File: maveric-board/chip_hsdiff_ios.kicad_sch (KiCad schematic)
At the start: 1 part, among them U1 Socket

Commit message: reannotate, fix all ERCs
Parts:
- renumbered U1 to U3
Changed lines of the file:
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@@
 		(dnp no)
 		(fields_autoplaced yes)
-		(property "Reference" "U1"
+		(property "Reference" "U3"
 			(at 134.62 17.78 0)
 			(effects
@@
 			(project ""
 				(path "/ae861d46-65fb-4872-932f-ad48addb0154/d741604b-a788-4cfa-8679-fc6e466b5431"
-					(reference "U1")
+					(reference "U3")
 					(unit 2)
 				)
@@
 		(dnp no)
 		(fields_autoplaced yes)
-		(property "Reference" "U1"
+		(property "Reference" "U3"
 			(at 54.61 17.78 0)
 			(effects
@@
 			(project ""
 				(path "/ae861d46-65fb-4872-932f-ad48addb0154/d741604b-a788-4cfa-8679-fc6e466b5431"
-					(reference "U1")
+					(reference "U3")
 					(unit 1)
 				)
@@
 		(dnp no)
 		(fields_autoplaced yes)
-		(property "Reference" "U1"
+		(property "Reference" "U3"
 			(at 134.62 104.14 0)
 			(effects
@@
 			(project ""
 				(path "/ae861d46-65fb-4872-932f-ad48addb0154/d741604b-a788-4cfa-8679-fc6e466b5431"
-					(reference "U1")
+					(reference "U3")
 					(unit 4)
 				)
@@
 		(dnp no)
 		(fields_autoplaced yes)
-		(property "Reference" "U1"
+		(property "Reference" "U3"
 			(at 222.25 17.78 0)
 			(effects
@@
 			(project ""
 				(path "/ae861d46-65fb-4872-932f-ad48addb0154/d741604b-a788-4cfa-8679-fc6e466b5431"
-					(reference "U1")
+					(reference "U3")
 					(unit 3)
 				)

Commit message: add uni2 socket footprint, check against drawing, fix npth, assign all footprints and part numbers
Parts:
- U3: footprint (none) -> maveric-parts:BGA-1733-.92-47.725x47.725
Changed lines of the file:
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@@
 			)
 		)
-		(property "Footprint" ""
+		(property "Footprint" "maveric-parts:BGA-1733-.92-47.725x47.725"
 			(at 96.52 24.13 0)
 			(effects
@@
 			)
 		)
-		(property "Footprint" ""
+		(property "Footprint" "maveric-parts:BGA-1733-.92-47.725x47.725"
 			(at 16.51 24.13 0)
 			(effects
@@
 			)
 		)
-		(property "Footprint" ""
+		(property "Footprint" "maveric-parts:BGA-1733-.92-47.725x47.725"
 			(at 96.52 110.49 0)
 			(effects
@@
 			)
 		)
-		(property "Footprint" ""
+		(property "Footprint" "maveric-parts:BGA-1733-.92-47.725x47.725"
 			(at 184.15 24.13 0)
 			(effects

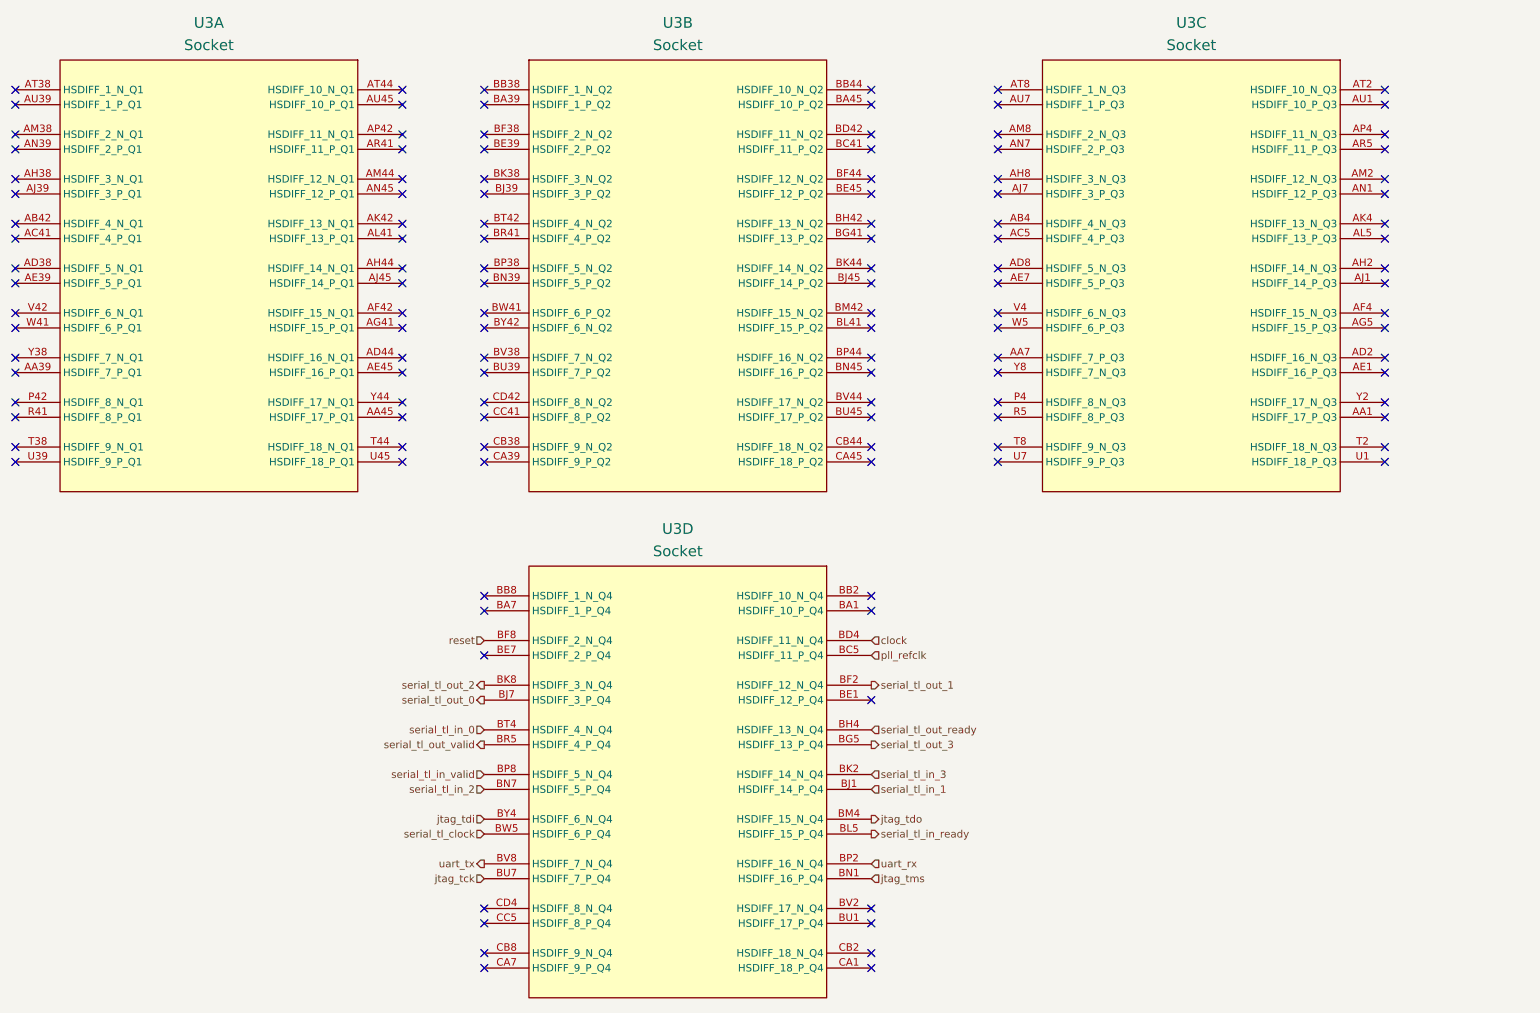
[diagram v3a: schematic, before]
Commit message: some docs + dnp uni2 socket
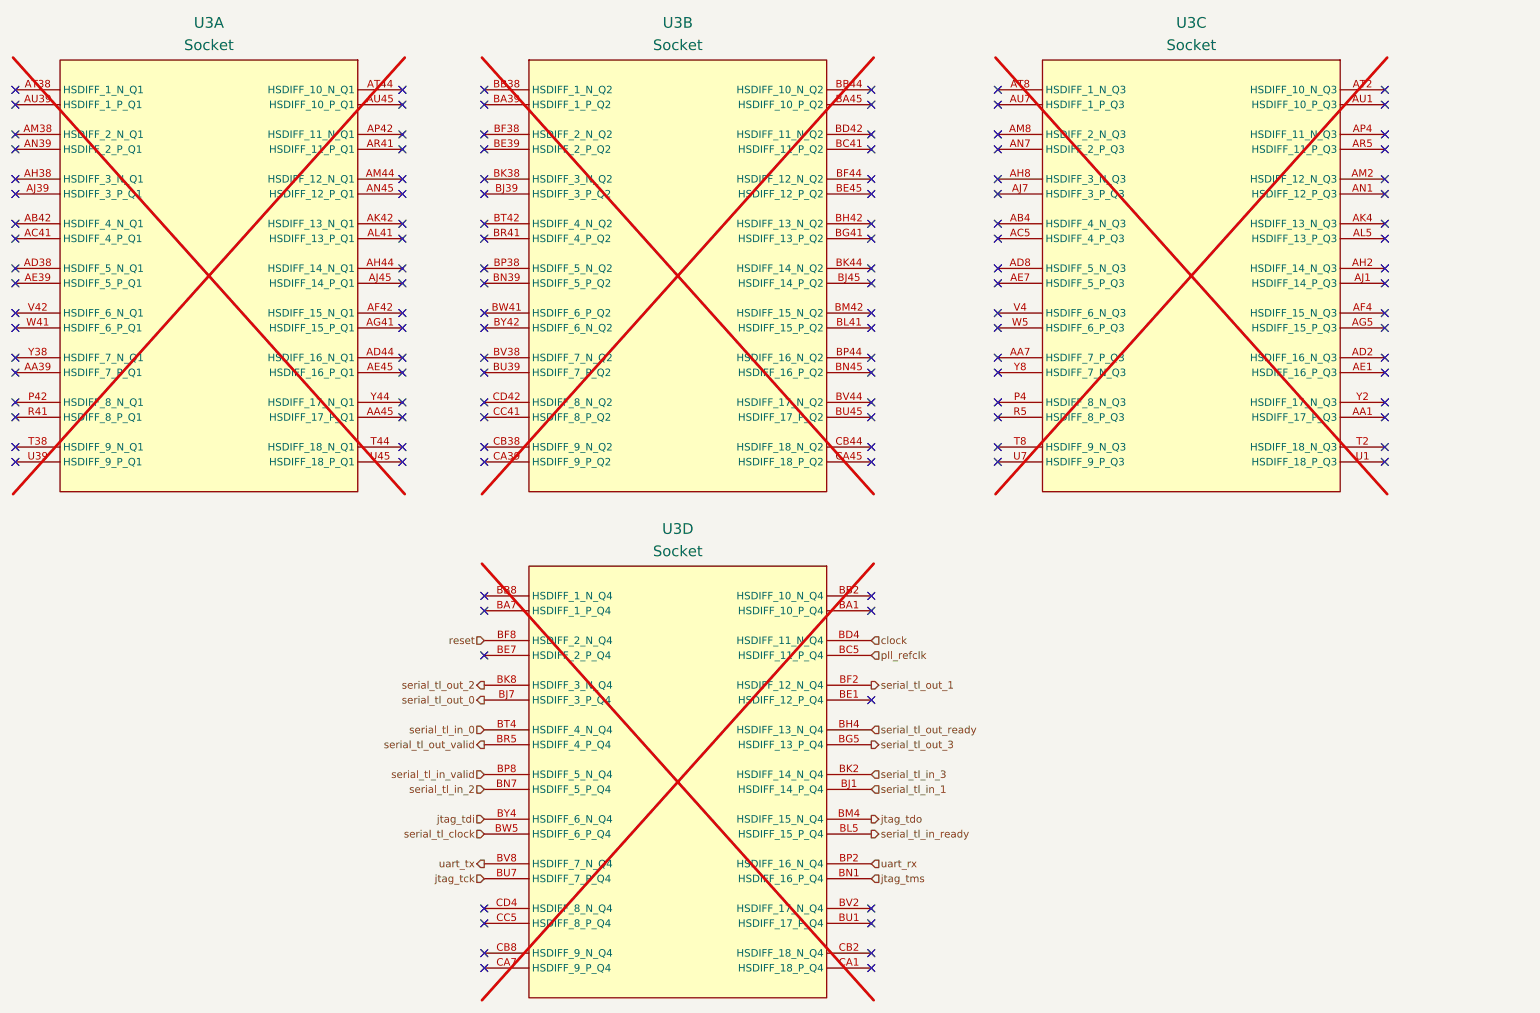
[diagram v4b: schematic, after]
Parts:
- U3: now not fitted
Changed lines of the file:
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@@
 		(in_bom yes)
 		(on_board yes)
-		(dnp no)
+		(dnp yes)
 		(fields_autoplaced yes)
 		(property "Reference" "U3"
@@
 		(in_bom yes)
 		(on_board yes)
-		(dnp no)
+		(dnp yes)
 		(fields_autoplaced yes)
 		(property "Reference" "U3"
@@
 		(in_bom yes)
 		(on_board yes)
-		(dnp no)
+		(dnp yes)
 		(fields_autoplaced yes)
 		(property "Reference" "U3"
@@
 		(in_bom yes)
 		(on_board yes)
-		(dnp no)
+		(dnp yes)
 		(fields_autoplaced yes)
 		(property "Reference" "U3"

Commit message: fix bump mapping
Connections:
- net clock: now also U3.AP4 (HSDIFF_11_N_Q3); no longer U3.BD4 (HSDIFF_11_N_Q4)
- net jtag_tck: now also U3.AA7 (HSDIFF_7_P_Q3); no longer U3.BU7 (HSDIFF_7_P_Q4)
- net jtag_tdi: now also U3.V4 (HSDIFF_6_N_Q3); no longer U3.BY4 (HSDIFF_6_N_Q4)
- net jtag_tdo: now also U3.AF4 (HSDIFF_15_N_Q3); no longer U3.BM4 (HSDIFF_15_N_Q4)
- net jtag_tms: now also U3.AE1 (HSDIFF_16_P_Q3); no longer U3.BN1 (HSDIFF_16_P_Q4)
- net pll_refclk: now also U3.AR5 (HSDIFF_11_P_Q3); no longer U3.BC5 (HSDIFF_11_P_Q4)
- net reset: now also U3.AM8 (HSDIFF_2_N_Q3); no longer U3.BF8 (HSDIFF_2_N_Q4)
- net serial_tl_clock: now also U3.W5 (HSDIFF_6_P_Q3); no longer U3.BW5 (HSDIFF_6_P_Q4)
- net serial_tl_in_0: now also U3.AB4 (HSDIFF_4_N_Q3); no longer U3.BT4 (HSDIFF_4_N_Q4)
- net serial_tl_in_1: now also U3.AJ1 (HSDIFF_14_P_Q3); no longer U3.BJ1 (HSDIFF_14_P_Q4)
- net serial_tl_in_2: now also U3.AE7 (HSDIFF_5_P_Q3); no longer U3.BN7 (HSDIFF_5_P_Q4)
- net serial_tl_in_3: now also U3.AH2 (HSDIFF_14_N_Q3); no longer U3.BK2 (HSDIFF_14_N_Q4)
- net serial_tl_in_ready: now also U3.AG5 (HSDIFF_15_P_Q3); no longer U3.BL5 (HSDIFF_15_P_Q4)
- net serial_tl_in_valid: now also U3.AD8 (HSDIFF_5_N_Q3); no longer U3.BP8 (HSDIFF_5_N_Q4)
- net serial_tl_out_0: now also U3.AJ7 (HSDIFF_3_P_Q3); no longer U3.BJ7 (HSDIFF_3_P_Q4)
- net serial_tl_out_1: now also U3.AM2 (HSDIFF_12_N_Q3); no longer U3.BF2 (HSDIFF_12_N_Q4)
- net serial_tl_out_2: now also U3.AH8 (HSDIFF_3_N_Q3); no longer U3.BK8 (HSDIFF_3_N_Q4)
- net serial_tl_out_3: now also U3.AL5 (HSDIFF_13_P_Q3); no longer U3.BG5 (HSDIFF_13_P_Q4)
- net serial_tl_out_ready: now also U3.AK4 (HSDIFF_13_N_Q3); no longer U3.BH4 (HSDIFF_13_N_Q4)
- net serial_tl_out_valid: now also U3.AC5 (HSDIFF_4_P_Q3); no longer U3.BR5 (HSDIFF_4_P_Q4)
- net uart_rx: now also U3.AD2 (HSDIFF_16_N_Q3); no longer U3.BP2 (HSDIFF_16_N_Q4)
- net uart_tx: now also U3.Y8 (HSDIFF_7_N_Q3); no longer U3.BV8 (HSDIFF_7_N_Q4)

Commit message: resync all symbols to schematic, reannotate schematic
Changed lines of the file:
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@@
 	(hierarchical_label "uart_tx"
 		(shape output)
+		(at 189.23 74.93 180)
+		(fields_autoplaced yes)
+		(effects
+			(font
+				(size 1.27 1.27)
+			)
+			(justify right)
+		)
+	)
+	(hierarchical_label "serial_tl_in_3"
+		(shape input)
+		(at 255.27 59.69 0)
+		(fields_autoplaced yes)
+		(effects
+			(font
+				(size 1.27 1.27)
+			)
+			(justify left)
+		)
+	)
+	(hierarchical_label "serial_tl_out_3"
+		(shape output)
+		(at 255.27 54.61 0)
+		(fields_autoplaced yes)
+		(effects
+			(font
+				(size 1.27 1.27)
+			)
+			(justify left)
+		)
+	)
+	(hierarchical_label "jtag_tdi"
+		(shape input)
+		(at 189.23 67.31 180)
+		(fields_autoplaced yes)
+		(effects
+			(font
+				(size 1.27 1.27)
+			)
+			(justify right)
+		)
+	)
+	(hierarchical_label "serial_tl_in_ready"
+		(shape output)
+		(at 255.27 69.85 0)
+		(fields_autoplaced yes)
+		(effects
+			(font
+				(size 1.27 1.27)
+			)
+			(justify left)
+		)
+	)
+	(hierarchical_label "serial_tl_out_0"
+		(shape output)
+		(at 189.23 46.99 180)
+		(fields_autoplaced yes)
+		(effects
+			(font
+				(size 1.27 1.27)
+			)
+			(justify right)
+		)
+	)
+	(hierarchical_label "serial_tl_in_2"
+		(shape input)
+		(at 189.23 62.23 180)
+		(fields_autoplaced yes)
+		(effects
+			(font
+				(size 1.27 1.27)
+			)
+			(justify right)
+		)
+	)
+	(hierarchical_label "serial_tl_out_valid"
+		(shape output)
+		(at 189.23 54.61 180)
+		(fields_autoplaced yes)
+		(effects
+			(font
+				(size 1.27 1.27)
+			)
+			(justify right)
+		)
+	)
+	(hierarchical_label "serial_tl_out_ready"
+		(shape input)
+		(at 255.27 52.07 0)
+		(fields_autoplaced yes)
+		(effects
+			(font
+				(size 1.27 1.27)
+			)
+			(justify left)
+		)
+	)
+	(hierarchical_label "reset"
+		(shape input)
+		(at 189.23 36.83 180)
+		(fields_autoplaced yes)
+		(effects
+			(font
+				(size 1.27 1.27)
+			)
+			(justify right)
+		)
+	)
+	(hierarchical_label "jtag_tms"
+		(shape input)
+		(at 255.27 77.47 0)
+		(fields_autoplaced yes)
+		(effects
+			(font
+				(size 1.27 1.27)
+			)
+			(justify left)
+		)
+	)
+	(hierarchical_label "serial_tl_out_2"
+		(shape output)
+		(at 189.23 44.45 180)
+		(fields_autoplaced yes)
+		(effects
+			(font
+				(size 1.27 1.27)
+			)
+			(justify right)
+		)
+	)
+	(hierarchical_label "serial_tl_clock"
+		(shape input)
+		(at 189.23 69.85 180)
+		(fields_autoplaced yes)
+		(effects
+			(font
+				(size 1.27 1.27)
+			)
+			(justify right)
+		)
+	)
+	(hierarchical_label "serial_tl_in_valid"
+		(shape input)
+		(at 189.23 59.69 180)
+		(fields_autoplaced yes)
+		(effects
+			(font
+				(size 1.27 1.27)
+			)
+			(justify right)
+		)
+	)
+	(hierarchical_label "uart_rx"
+		(shape input)
+		(at 255.27 74.93 0)
+		(fields_autoplaced yes)
+		(effects
+			(font
+				(size 1.27 1.27)
+			)
+			(justify left)
+		)
+	)
+	(hierarchical_label "serial_tl_in_0"
+		(shape input)
+		(at 189.23 52.07 180)
+		(fields_autoplaced yes)
+		(effects
+			(font
+				(size 1.27 1.27)
+			)
+			(justify right)
+		)
+	)
+	(hierarchical_label "serial_tl_in_1"
+		(shape input)
+		(at 255.27 62.23 0)
+		(fields_autoplaced yes)
+		(effects
+			(font
+				(size 1.27 1.27)
+			)
+			(justify left)
+		)
+	)
+	(hierarchical_label "pll_refclk"
+		(shape input)
+		(at 255.27 39.37 0)
+		(fields_autoplaced yes)
+		(effects
+			(font
+				(size 1.27 1.27)
+			)
+			(justify left)
+		)
+	)
+	(hierarchical_label "jtag_tck"
+		(shape input)
 		(at 189.23 77.47 180)
 		(fields_autoplaced yes)
 		(effects
-			(font
-				(size 1.27 1.27)
-			)
-			(justify right)
-		)
-	)
-	(hierarchical_label "serial_tl_in_3"
-		(shape input)
-		(at 255.27 59.69 0)
-		(fields_autoplaced yes)
-		(effects
-			(font
-				(size 1.27 1.27)
-			)
-			(justify left)
-		)
-	)
-	(hierarchical_label "serial_tl_out_3"
-		(shape output)
-		(at 255.27 54.61 0)
-		(fields_autoplaced yes)
-		(effects
-			(font
-				(size 1.27 1.27)
-			)
-			(justify left)
-		)
-	)
-	(hierarchical_label "jtag_tdi"
-		(shape input)
-		(at 189.23 67.31 180)
-		(fields_autoplaced yes)
-		(effects
-			(font
-				(size 1.27 1.27)
-			)
-			(justify right)
-		)
-	)
-	(hierarchical_label "serial_tl_in_ready"
-		(shape output)
-		(at 255.27 69.85 0)
-		(fields_autoplaced yes)
-		(effects
-			(font
-				(size 1.27 1.27)
-			)
-			(justify left)
-		)
-	)
-	(hierarchical_label "serial_tl_out_0"
-		(shape output)
-		(at 189.23 46.99 180)
-		(fields_autoplaced yes)
-		(effects
-			(font
-				(size 1.27 1.27)
-			)
-			(justify right)
-		)
-	)
-	(hierarchical_label "serial_tl_in_2"
-		(shape input)
-		(at 189.23 62.23 180)
-		(fields_autoplaced yes)
-		(effects
-			(font
-				(size 1.27 1.27)
-			)
-			(justify right)
-		)
-	)
-	(hierarchical_label "serial_tl_out_valid"
-		(shape output)
-		(at 189.23 54.61 180)
-		(fields_autoplaced yes)
-		(effects
-			(font
-				(size 1.27 1.27)
-			)
-			(justify right)
-		)
-	)
-	(hierarchical_label "serial_tl_out_ready"
-		(shape input)
-		(at 255.27 52.07 0)
-		(fields_autoplaced yes)
-		(effects
-			(font
-				(size 1.27 1.27)
-			)
-			(justify left)
-		)
-	)
-	(hierarchical_label "reset"
-		(shape input)
-		(at 189.23 36.83 180)
-		(fields_autoplaced yes)
-		(effects
-			(font
-				(size 1.27 1.27)
-			)
-			(justify right)
-		)
-	)
-	(hierarchical_label "jtag_tms"
-		(shape input)
-		(at 255.27 77.47 0)
-		(fields_autoplaced yes)
-		(effects
-			(font
-				(size 1.27 1.27)
-			)
-			(justify left)
-		)
-	)
-	(hierarchical_label "serial_tl_out_2"
-		(shape output)
-		(at 189.23 44.45 180)
-		(fields_autoplaced yes)
-		(effects
-			(font
-				(size 1.27 1.27)
-			)
-			(justify right)
-		)
-	)
-	(hierarchical_label "serial_tl_clock"
-		(shape input)
-		(at 189.23 69.85 180)
-		(fields_autoplaced yes)
-		(effects
-			(font
-				(size 1.27 1.27)
-			)
-			(justify right)
-		)
-	)
-	(hierarchical_label "serial_tl_in_valid"
-		(shape input)
-		(at 189.23 59.69 180)
-		(fields_autoplaced yes)
-		(effects
-			(font
-				(size 1.27 1.27)
-			)
-			(justify right)
-		)
-	)
-	(hierarchical_label "uart_rx"
-		(shape input)
-		(at 255.27 74.93 0)
-		(fields_autoplaced yes)
-		(effects
-			(font
-				(size 1.27 1.27)
-			)
-			(justify left)
-		)
-	)
-	(hierarchical_label "serial_tl_in_0"
-		(shape input)
-		(at 189.23 52.07 180)
-		(fields_autoplaced yes)
-		(effects
-			(font
-				(size 1.27 1.27)
-			)
-			(justify right)
-		)
-	)
-	(hierarchical_label "serial_tl_in_1"
-		(shape input)
-		(at 255.27 62.23 0)
-		(fields_autoplaced yes)
-		(effects
-			(font
-				(size 1.27 1.27)
-			)
-			(justify left)
-		)
-	)
-	(hierarchical_label "pll_refclk"
-		(shape input)
-		(at 255.27 39.37 0)
-		(fields_autoplaced yes)
-		(effects
-			(font
-				(size 1.27 1.27)
-			)
-			(justify left)
-		)
-	)
-	(hierarchical_label "jtag_tck"
-		(shape input)
-		(at 189.23 74.93 180)
-		(fields_autoplaced yes)
-		(effects

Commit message: fixup schematic + redo banana jack footprints to match jlc render
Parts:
- U3: value Socket -> Testchip socket
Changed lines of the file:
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@@
 			)
 		)
-		(property "Value" "Socket"
+		(property "Value" "Testchip socket"
 			(at 134.62 21.59 0)
 			(effects
@@
 			)
 		)
-		(property "Value" "Socket"
+		(property "Value" "Testchip socket"
 			(at 54.61 21.59 0)
 			(effects
@@
 			)
 		)
-		(property "Value" "Socket"
+		(property "Value" "Testchip socket"
 			(at 134.62 107.95 0)
 			(effects
@@
 			)
 		)
-		(property "Value" "Socket"
+		(property "Value" "Testchip socket"
 			(at 222.25 21.59 0)
 			(effects
